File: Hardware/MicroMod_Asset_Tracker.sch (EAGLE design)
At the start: 198 parts, among them J11 microSD, J13 TP, J17 NANO_SIM, J18 SARA_USB, J19 NI, J2 JTAG, J4 MICROMOD-2222-C, J5 SPI, J6 SPI, J7 QWIIC_RIGHT_ANGLE, J9 !RST!, Q1 310mA/60V/1.6Ω, Q10 20V/0.2A/8MHz/1.2Ω/1Vth, Q2 310mA/60V/1.6Ω, Q3 310mA/60V/1.6Ω, Q4 310mA/60V/1.6Ω, Q5 20V/0.2A/8MHz/1.2Ω/1Vth, Q6 20V/4.2A/52mΩ/1.4W, Q7 310mA/60V/1.6Ω, U1 SARA-R5, U13 9DoF IMU, U14 1.8V/100mA, U2 MCP73831, U3 3.3V, U4 TXB0104, U5 AP7361C-33FGE, U6 TXB0104, U7 PCA9306, U8 74HC1G04, U9 TXB0104

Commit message: Ready for review
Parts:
- added TP13, TP22, TP23, TP24: TEST-POINT3, SparkFun-Connectors:TEST-POINT3
- J1: device SparkFun-Connectors:USB_C_2-LAYER_PADS -> SparkFun-Connectors:USB_C_4-LAYER_PADS
- J6: value SPI -> DIAG
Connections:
- net N$19 renamed G0
- net N$40 renamed G1
- net N$41 renamed G2
- net N$42 renamed G3
- net N$43 renamed G4
- net N$44 renamed G5
- net N$45 renamed G6
- net N$46 renamed G7
- net N$48 renamed G10
- net N$50 renamed G9
- removed net SARA_ON: JP19.2, JP21.2, Q7.D, R43.1, R44.1
- new net SARA_!ON!: JP19.2, JP21.2, Q7.D, R43.1, R44.1, TP13.1
- net N$14: now also TP24.1
- net N$25: now also TP22.1
- net SD_PWR: now also TP23.1
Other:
- note added: "Prepreg dielectric thickness (layer 1 to 2): 0.2mm"
- note added: "SARA ANT and ANT_GNSS pads do not require restrict on layer 2 as the prepreg thickness is >= 200µm"
- note removed: "Dielectric thickness (layer 1 to 2): 0.2mm"
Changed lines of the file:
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@@
 <parts>
 <part name="FRAME1" library="SparkFun-Aesthetics" deviceset="FRAME-LEDGER" device=""/>
-<part name="J1" library="SparkFun-Connectors" deviceset="USB_C" device="_2-LAYER_PADS"/>
+<part name="J1" library="SparkFun-Connectors" deviceset="USB_C" device="_4-LAYER_PADS"/>
 <part name="R2" library="SparkFun-Resistors" deviceset="5.1KOHM" device="5.1KOHM-0603-1/10W-1%" value="5.1k"/>
 <part name="R3" library="SparkFun-Resistors" deviceset="5.1KOHM" device="5.1KOHM-0603-1/10W-1%" value="5.1k"/>
@@
 <part name="R30" library="SparkFun-Resistors" deviceset="2.2KOHM" device="-0603-1/10W-1%" value="2.2k"/>
 <part name="SUPPLY42" library="SparkFun-PowerSymbols" deviceset="3.3V" device=""/>
-<part name="J6" library="SparkFun-Connectors" deviceset="CONN_05" device="NO_SILK" value="SPI"/>
+<part name="J6" library="SparkFun-Connectors" deviceset="CONN_05" device="NO_SILK" value="DIAG"/>
 <part name="GND17" library="SparkFun-PowerSymbols" deviceset="GND" device=""/>
 <part name="SUPPLY44" library="SparkFun-PowerSymbols" deviceset="VIN" device=""/>
@@
 <part name="JP19" library="SparkFun-Jumpers" deviceset="JUMPER-SMT_2_NC_TRACE" device="_SILK" package3d_urn="urn:adsk.eagle:package:39281/1"/>
 <part name="JP21" library="SparkFun-Jumpers" deviceset="JUMPER-SMT_2_NO" device="_SILK" package3d_urn="urn:adsk.eagle:package:39279/1"/>
+<part name="TP13" library="SparkFun-Connectors" deviceset="TEST-POINT" device="3" value="TEST-POINT3"/>
+<part name="TP22" library="SparkFun-Connectors" deviceset="TEST-POINT" device="3" value="TEST-POINT3"/>
+<part name="TP23" library="SparkFun-Connectors" deviceset="TEST-POINT" device="3" value="TEST-POINT3"/>
+<part name="TP24" library="SparkFun-Connectors" deviceset="TEST-POINT" device="3" value="TEST-POINT3"/>
 </parts>
 <sheets>
@@
 <attribute name="NAME" x="130.048" y="23.241" size="1.778" layer="95" font="vector"/>
 </instance>
+<instance part="TP23" gate="G$1" x="300.99" y="260.35" smashed="yes" rot="R90">
+<attribute name="NAME" x="299.72" y="257.81" size="1.778" layer="95" font="vector" rot="R90"/>
+</instance>
+<instance part="TP24" gate="G$1" x="359.41" y="181.61" smashed="yes" rot="R90">
+<attribute name="NAME" x="358.14" y="179.07" size="1.778" layer="95" font="vector" rot="R90"/>
+</instance>
 </instances>
 <busses>
@@
 <wire x1="373.38" y1="180.34" x2="373.38" y2="185.42" width="0.1524" layer="91"/>
 <junction x="365.76" y="180.34"/>
+<pinref part="TP24" gate="G$1" pin="1"/>
+<wire x1="359.41" y1="181.61" x2="359.41" y2="180.34" width="0.1524" layer="91"/>
+<wire x1="359.41" y1="180.34" x2="365.76" y2="180.34" width="0.1524" layer="91"/>
 </segment>
 </net>
@@
 <pinref part="J11" gate="G$1" pin="VCC"/>
 <wire x1="292.1" y1="248.92" x2="292.1" y2="254" width="0.1524" layer="91"/>
-<wire x1="312.42" y1="256.54" x2="297.18" y2="256.54" width="0.1524" layer="91"/>
+<wire x1="312.42" y1="256.54" x2="300.99" y2="256.54" width="0.1524" layer="91"/>
+<wire x1="300.99" y1="256.54" x2="297.18" y2="256.54" width="0.1524" layer="91"/>
 <wire x1="297.18" y1="256.54" x2="297.18" y2="248.92" width="0.1524" layer="91"/>
 <wire x1="297.18" y1="248.92" x2="292.1" y2="248.92" width="0.1524" layer="91"/>
@@
 <wire x1="292.1" y1="243.84" x2="292.1" y2="248.92" width="0.1524" layer="91"/>
 <junction x="292.1" y="248.92"/>
+<pinref part="TP23" gate="G$1" pin="1"/>
+<wire x1="300.99" y1="256.54" x2="300.99" y2="260.35" width="0.1524" layer="91"/>
+<junction x="300.99" y="256.54"/>
 </segment>
 </net>
@@
 </segment>
 </net>
-<net name="N$19" class="0">
+<net name="G0" class="0">
 <segment>
 <pinref part="J4" gate="J1" pin="G0/BUS0"/>
@@
 </segment>
 </net>
-<net name="N$40" class="0">
+<net name="G1" class="0">
 <segment>
 <pinref part="J4" gate="J1" pin="G1/BUS1"/>
@@
 </segment>
 </net>
-<net name="N$41" class="0">
+<net name="G2" class="0">
 <segment>
 <pinref part="J4" gate="J1" pin="G2/BUS2"/>
@@
 </segment>
 </net>
-<net name="N$42" class="0">
+<net name="G3" class="0">
 <segment>
 <pinref part="J4" gate="J1" pin="G3/BUS3"/>
@@
 </segment>
 </net>
-<net name="N$43" class="0">
+<net name="G4" class="0">
 <segment>
 <pinref part="J4" gate="J1" pin="G4/BUS4"/>
@@
 </segment>
 </net>
-<net name="N$44" class="0">
+<net name="G5" class="0">
 <segment>
 <pinref part="J4" gate="J1" pin="G5/BUS5"/>
@@
 </segment>
 </net>
-<net name="N$45" class="0">
+<net name="G6" class="0">
 <segment>
 <pinref part="J4" gate="J1" pin="G6/BUS6"/>
@@
 </segment>
 </net>
-<net name="N$46" class="0">
+<net name="G7" class="0">
 <segment>
 <pinref part="J4" gate="J1" pin="G7/BUS7"/>
@@
 </segment>
 </net>
-<net name="SARA_ON" class="0">
+<net name="SARA_!ON!" class="0">
 <segment>
 <wire x1="144.78" y1="22.86" x2="147.32" y2="22.86" width="0.1524" layer="91"/>
@@
 </segment>
 </net>
-<net name="N$48" class="0">
+<net name="G10" class="0">
 <segment>
 <pinref part="J4" gate="J1" pin="G10/ADC_D+/CAM_VSYNC"/>
@@
 </segment>
 </net>
-<net name="N$50" class="0">
+<net name="G9" class="0">
 <segment>
 <pinref part="J4" gate="J1" pin="G9/ADC_D-/CAM_HSYNC"/>
@@
 <text x="351.028" y="11.43" size="2.54" layer="94">Paul Clark</text>
 <text x="421.64" y="7.112" size="2.54" layer="94">v10</text>
-<text x="101.346" y="266.192" size="1.27" layer="97">Board thickness: 1.6mm</text>
-<text x="101.346" y="261.112" size="1.27" layer="97">Er: 4.6</text>
-<text x="101.346" y="268.732" size="1.27" layer="97">Copper Thickness (1oz): 1.4mil/0.035mm</text>
-<text x="101.346" y="256.032" size="1.27" layer="97">RF Trace Width: 13.8mil/0.35mm</text>
-<text x="101.346" y="258.572" size="1.27" layer="97">Polygon Isolation: 8mil/0.2032mm</text>
-<text x="101.346" y="263.652" size="1.27" layer="97">Dielectric thickness (layer 1 to 2): 0.2mm</text>
-<text x="101.346" y="253.492" size="0.762" layer="97">https://chemandy.com/calculators/coplanar-waveguide-with-ground-calculator.htm</text>
-<text x="101.346" y="271.272" size="1.524" layer="97" ratio="15">Microstrip Calculation:</text>
+<text x="98.806" y="268.732" size="1.27" layer="97">Board thickness: 1.6mm</text>
+<text x="98.806" y="263.652" size="1.27" layer="97">Er: 4.6</text>
+<text x="98.806" y="271.272" size="1.27" layer="97">Copper Thickness (1oz): 1.4mil/0.035mm</text>
+<text x="98.806" y="258.572" size="1.27" layer="97">RF Trace Width: 13.8mil/0.35mm</text>
+<text x="98.806" y="261.112" size="1.27" layer="97">Polygon Isolation: 8mil/0.2032mm</text>
+<text x="98.806" y="266.192" size="1.27" layer="97">Prepreg dielectric thickness (layer 1 to 2): 0.2mm</text>
+<text x="98.806" y="256.032" size="0.762" layer="97">https://chemandy.com/calculators/coplanar-waveguide-with-ground-calculator.htm</text>
+<text x="98.806" y="273.812" size="1.524" layer="97" ratio="15">Microstrip Calculation:</text>
 <wire x1="91.44" y1="279.4" x2="91.44" y2="200.66" width="0.2032" layer="97" style="longdash"/>
 <text x="27.94" y="261.62" size="2.54" layer="97">50Ω</text>
@@
 <wire x1="210.82" y1="200.66" x2="210.82" y2="134.62" width="0.2032" layer="97" style="longdash"/>
 <wire x1="431.8" y1="134.62" x2="210.82" y2="134.62" width="0.2032" layer="97" style="longdash"/>
+<text x="98.806" y="250.952" size="1.27" layer="97">SARA ANT and ANT_GNSS pads do not require restrict on layer 2
+as the prepreg thickness is &gt;= 200µm</text>
 </plain>
 <instances>
@@
 <attribute name="VALUE" x="182.88" y="178.054" size="1.778" layer="96" font="vector" align="bottom-center"/>
 </instance>
+<instance part="TP13" gate="G$1" x="167.64" y="162.56" smashed="yes" rot="R90">
+<attribute name="NAME" x="166.37" y="160.02" size="1.778" layer="95" font="vector" rot="R90"/>
+</instance>
+<instance part="TP22" gate="G$1" x="195.58" y="238.76" smashed="yes" rot="R90">
+<attribute name="NAME" x="194.31" y="236.22" size="1.778" layer="95" font="vector" rot="R90"/>
+</instance>
 </instances>
 <busses>
@@
 <wire x1="190.5" y1="231.14" x2="190.5" y2="233.68" width="0.1524" layer="91"/>
 <junction x="190.5" y="233.68"/>
+<pinref part="TP22" gate="G$1" pin="1"/>
+<wire x1="195.58" y1="238.76" x2="195.58" y2="233.68" width="0.1524" layer="91"/>
+<wire x1="195.58" y1="233.68" x2="190.5" y2="233.68" width="0.1524" layer="91"/>
 </segment>
 </net>
@@
 </segment>
 </net>
-<net name="SARA_ON" class="0">
+<net name="SARA_!ON!" class="0">
 <segment>
 <pinref part="Q7" gate="NMOS" pin="D"/>
@@
 <wire x1="182.88" y1="162.56" x2="182.88" y2="160.02" width="0.1524" layer="91"/>
 <junction x="182.88" y="160.02"/>
+<pinref part="TP13" gate="G$1" pin="1"/>
+<wire x1="167.64" y1="162.56" x2="167.64" y2="160.02" width="0.1524" layer="91"/>
+<wire x1="167.64" y1="160.02" x2="175.26" y2="160.02" width="0.1524" layer="91"/>
 </segment>
 </net>

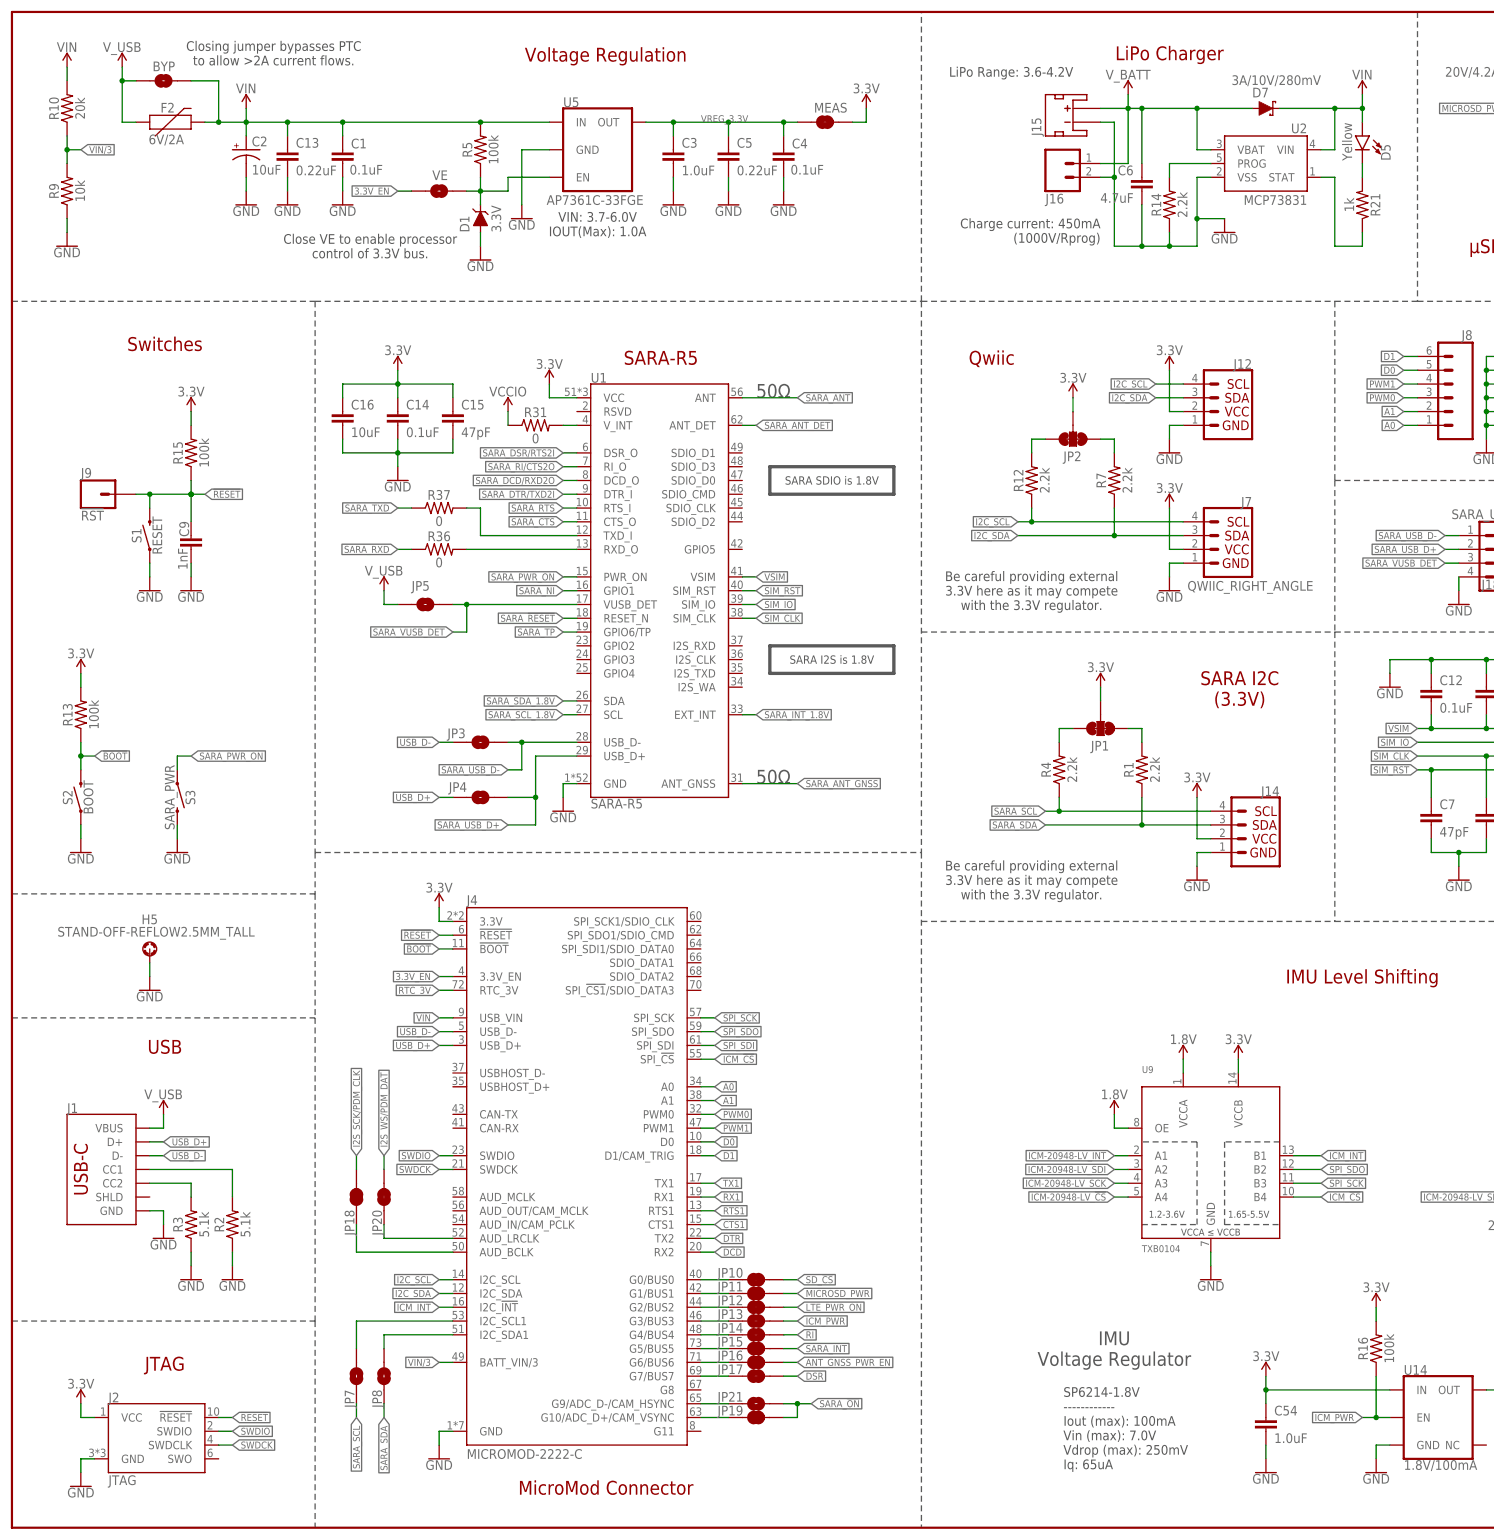
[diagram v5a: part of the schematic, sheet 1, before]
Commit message: Replaced the Level Shifters
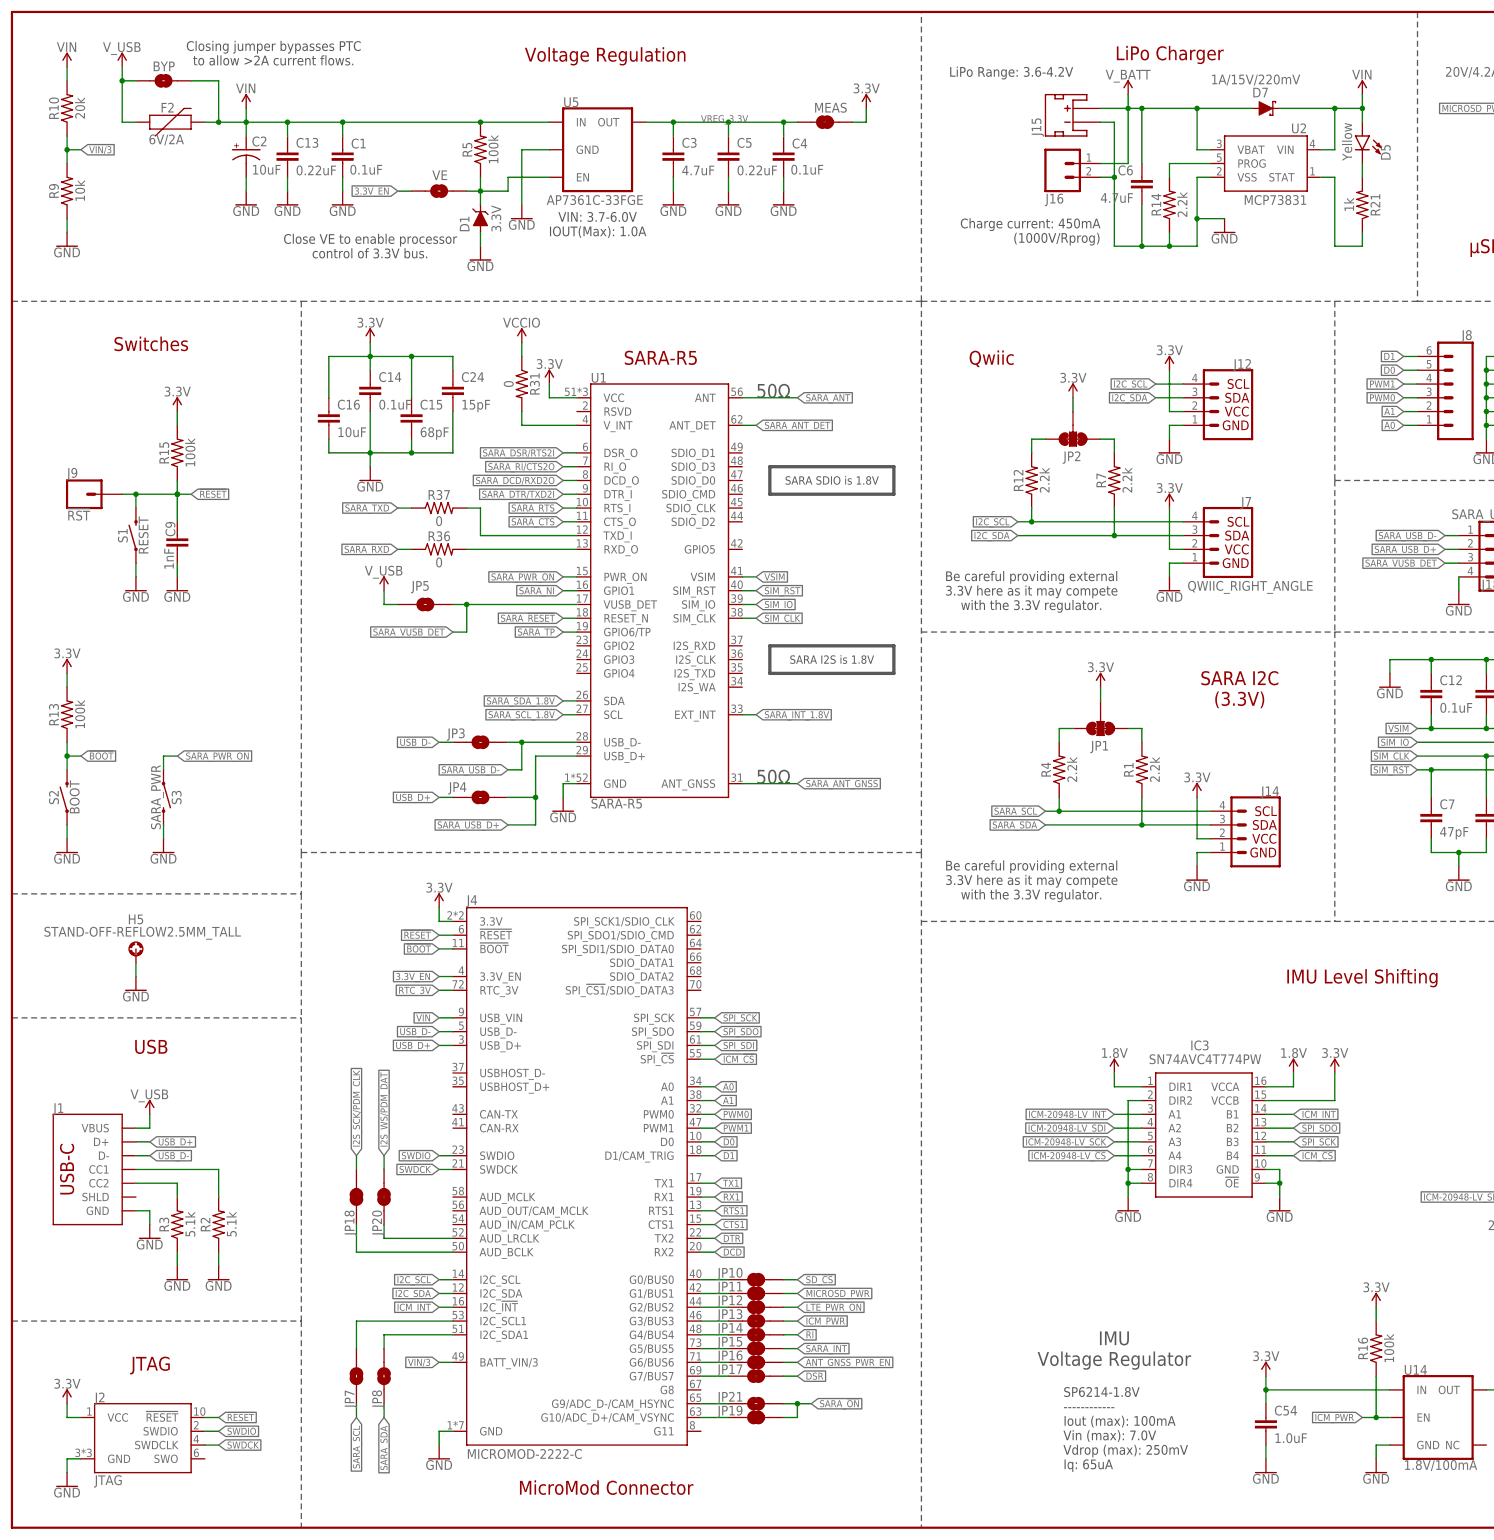
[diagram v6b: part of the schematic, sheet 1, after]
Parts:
- removed JP9: JUMPER-SMT_2_NO_SILK, SparkFun-Jumpers:JUMPER-SMT_2_NO_SILK
- removed U4, U6, U9: TXB0104, SparkFun-IC-Comms:TXB0104PWR
- added C24: 15pF, SparkFun-Capacitors:15PF-0603-50V-5%
- added IC1, IC2, IC3: SN74AVC4T774PW, New_Parts:SN74AVC4T774PW
- added JP22: JUMPER-SMT_3_1-NC_TRACE_SILK, SparkFun-Jumpers:JUMPER-SMT_3_1-NC_TRACE_SILK
- C15: value 47pF -> 68pF; device SparkFun-Capacitors:47PF-0603-50V-5% -> SparkFun-Capacitors:68PF-0603-50V-5%
- C3: value 1.0uF -> 4.7uF; device SparkFun-Capacitors:1.0UF-0603-16V-10% -> SparkFun-Capacitors:4.7UF-0603-6.3V-(10%)
- D7: value 3A/10V/280mV -> 1A/15V/220mV; device SparkFun-DiscreteSemi:DIODE-SCHOTTKY-BAT60A -> SparkFun-DiscreteSemi:DIODE-SCHOTTKY-LSM115JE3
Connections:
- removed net N$18: JP9.2, R20.1
- new net N$23: IC2.DIR4, JP22.2
- net 1.8V: now also IC3.DIR1, IC3.VCCA; no longer U9.OE, U9.VCCA
- net 3.3V: now also C24.1, IC1.VCCB, IC2.VCCB, IC3.VCCB; no longer U4.VCCB, U6.VCCB, U9.VCCB
- net CTS1: now also IC1.B3; no longer U4.B3
- net DCD: now also IC2.B2; no longer U6.B2
- net DSR: now also IC2.B4; no longer U6.B4
- net DTR: now also IC2.B1; no longer U6.B1
- net GND: now also C24.2, IC1.!OE, IC1.DIR2, IC1.DIR4, IC1.GND, IC2.!OE, IC2.DIR1, IC2.GND, IC3.!OE, IC3.DIR2, IC3.DIR3, IC3.DIR4, IC3.GND, JP22.1, R20.1; no longer JP9.1, U4.GND, U6.GND, U9.GND
- net ICM-20948-LV_!CS!: now also IC3.A4; no longer U9.A4
- net ICM-20948-LV_INT: now also IC3.A1; no longer U9.A1
- net ICM-20948-LV_SCK: now also IC3.A3; no longer U9.A3
- net ICM-20948-LV_SDI: now also IC3.A2; no longer U9.A2
- net ICM_!CS!: now also IC3.B4; no longer U9.B4
- net ICM_INT: now also IC3.B1; no longer U9.B1
- net RI: now also IC2.B3; no longer U6.B3
- net RTS1: now also IC1.B4; no longer U4.B4
- net RX1: now also IC1.B1; no longer U4.B1
- net SARA_CTS: now also IC1.A3; no longer U4.A3
- net SARA_DCD/RXD2O: now also IC2.A2; no longer U6.A2
- net SARA_DSR/RTS2I: now also IC2.A4; no longer U6.A4
- net SARA_DTR/TXD2I: now also IC2.A1; no longer U6.A1
- net SARA_RI/CTS2O: now also IC2.A3; no longer U6.A3
- net SARA_RTS: now also IC1.A4; no longer U4.A4
- net SARA_RXD: now also IC1.A1; no longer U4.A1
- net SARA_TXD: now also IC1.A2; no longer U4.A2
- net SPI_SCK: now also IC3.B3; no longer U9.B3
- net SPI_SDO: now also IC3.B2; no longer U9.B2
- net TX1: now also IC1.B2; no longer U4.B2
- net VCCIO: now also IC1.DIR1, IC1.DIR3, IC1.VCCA, IC2.DIR2, IC2.DIR3, IC2.VCCA, JP22.3; no longer U4.OE, U4.VCCA, U6.OE, U6.VCCA
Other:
- note added: "AP2112K-3.3V 3.3V @ 600mA Iq = 50µA"
- note added: "SARA-R5 VCC Design Notes:"
- note added: "VCC: Min. 3.3V Typ. 3.8V Max. 4.4V VCC Extended: Min. 3.0V Max. 4.5V Worst case: Maximum current draw during Tx: 395mA Estimated current for other components: 100mA Total maximum current draw: ~500mA AP7361C-33 drop out voltage: ~170mV at: 500mA output current; Vout = 3.3V; 25°C D7 LSM115J Schottky diode forward voltage: ~210mV at: 500mA; 25°C AP7361C 3.3V output will start to fall when the batte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"
- moved on the sheet: C14, C15, C16, C22, C23, C9, H5, J1, J2, J9, R13, R15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

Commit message: Ready for review
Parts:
- added U$132: MAX17048, SparkFun-IC-Power:MAX17048DFN8
- renumbered JP22 to DSR
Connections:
- net GND: now also U$132.CTG, U$132.GND, U$132.QSTRT
- net I2C_SCL: now also U$132.SCL
- net I2C_SDA: now also U$132.SDA
- net V_BATT: now also U$132.CELL, U$132.VDD
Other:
- note added: "Battery Fuel Gauge"
- note added: "Change jumper to reverse the direction of DSR for 2 UART communication"
- note added: "I2C Address = 0x36"
